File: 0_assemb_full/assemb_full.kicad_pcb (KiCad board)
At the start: 2 copper layers, 100.3 x 100.3 mm, 147 parts, among them J1 BarrelJack, J10 SPIConn_01x03, J11 OutToRPi, J2 Conn_02x06, J3 AudioJack3, J4 Servo0Conn_01x03, J5 Servo1Conn_01x03, J6 Servo2Conn_01x03, J7 Servo3Conn_01x03, J8 Servo4Conn_01x03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

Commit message: Pre-STM32 portion rework
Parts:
- added C50: 0.1u, Capacitor_SMD:C_0805_2012Metric_Pad1.18x1.45mm_HandSolder, B.Cu at (69.8, 100.0)
- added REF**: SolderJumper-2_P1.3mm_Open_Pad1.0x1.5mm, Jumper:SolderJumper-2_P1.3mm_Open_Pad1.0x1.5mm, F.Cu at (109.4, 113.2)
- added U7: MAX7375AXR805, Package_TO_SOT_SMD:SOT-323_SC-70, B.Cu at (67.4, 100.0)
- H1, H2, H3, H4: footprint MountingHole:MountingHole_6.4mm_M6 -> MountingHole:MountingHole_3.2mm_M3
- R5, R9: moved to B.Cu
- moved R3 247.7 mm to (13.6, 148.3)
- moved R2 247.7 mm to (23.5, 142.2)
- moved TP9 247.1 mm to (25.5, 149.0)
- moved TP7 205.9 mm to (45.9, 93.7)
- moved TP3 195.9 mm to (63.0, 115.7)
- moved TP1 188.3 mm to (60.3, 111.2)
- moved TP8 187.6 mm to (76.7, 145.1), turned to -90 degrees
- moved TP2 186.5 mm to (60.4, 115.3)
- moved TP5 184.0 mm to (57.6, 120.0)
- moved R8 178.4 mm to (79.0, 150.1), turned to 90 degrees
- moved TP4 175.2 mm to (60.5, 118.6)
- moved R5 173.8 mm to (70.8, 141.2), turned to -90 degrees
- moved R1 171.9 mm to (70.1, 144.9), turned to 180 degrees
- moved TP6 169.2 mm to (59.1, 108.5)
- moved R9 158.8 mm to (74.2, 139.8), turned to 180 degrees
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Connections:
- U5 pad 5: unconnected-(U5-Pad5) -> /STM32 Interface/EClock
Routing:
- net Filter_In: track 0.00 -> 29.7 mm
- net 5V: track 167.1 -> 194.0 mm
- net Audio_In_Ring: track 0.00 -> 21.5 mm
- net 3_3V: track 100.2 -> 119.2 mm
- net Net-(TP5-Pad1): track 0.00 -> 18.5 mm
- net ADC_LP: track 0.00 -> 17.9 mm
- net Net-(TP4-Pad1): track 0.00 -> 15.0 mm
- net ADC_BP: track 0.00 -> 14.6 mm
- net ADC_HP: track 0.00 -> 11.9 mm
- net GND: track 58.1 -> 69.7 mm, vias 4 -> 9
- net Audio_In_Tip: track 0.00 -> 11.5 mm
- net /Bandpass/LP Pre-LP: track 0.00 -> 10.7 mm
- net Net-(TP3-Pad1): track 0.00 -> 10.2 mm
- net Net-(C5-Pad2): track 0.00 -> 9.66 mm
- net Net-(C4-Pad2): track 0.00 -> 7.68 mm
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- added copper zone on F.Cu, net (none)
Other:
- board text added: "Change electrolytic to 0805"
- board text added: "Micro to the right Power and servo connections to the left"
- board text added: "Use two big vias instead of multiples"

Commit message: Additional changes
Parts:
- C13, C17, C19, C22, C23, C36, C37, C38, C39: footprint Capacitor_THT:CP_Radial_D5.0mm_P2.50mm -> Capacitor_SMD:C_0805_2012Metric_Pad1.18x1.45mm_HandSolder
- C2: footprint Capacitor_THT:CP_Radial_D5.0mm_P2.00mm -> Capacitor_SMD:C_0805_2012Metric_Pad1.18x1.45mm_HandSolder
- R10, R11, R6, R7: moved to B.Cu
- moved R11 206.9 mm to (61.4, 136.7)
- moved R7 194.5 mm to (65.6, 136.7)
- moved R6 183.2 mm to (88.6, 143.9)
- moved R10 169.8 mm to (84.6, 143.9)
- moved R3 67.4 mm to (80.9, 151.0), turned to 90 degrees
- moved TP9 67.0 mm to (92.5, 147.2)
- moved C3 63.7 mm to (90.8, 151.6), turned to 180 degrees
- moved R2 60.2 mm to (83.0, 151.1), turned to -90 degrees
- moved C7 60.0 mm to (81.5, 157.6)
- moved U4 6.15 mm to (91.5, 162.6)
- moved R1 4.91 mm to (70.1, 149.8)
- moved R23 4.91 mm to (59.5, 159.6)
- moved R5 4.91 mm to (70.8, 146.1)
- moved R8 4.91 mm to (79.1, 155.0)
- moved R9 4.91 mm to (74.2, 144.7)
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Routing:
- net Net-(C3-Pad1): track 0.00 -> 42.2 mm
- net Net-(C7-Pad2): track 0.00 -> 14.4 mm
- net 5V: track 194.0 -> 199.8 mm
- net Net-(R10-Pad2): track 0.00 -> 5.49 mm
- net Net-(R11-Pad2): track 0.00 -> 5.27 mm
- net Net-(C3-Pad2): track 0.00 -> 5.08 mm
- net /Bandpass/LP Pre-LP: track 10.7 -> 15.0 mm, vias 0 -> 1
- net Net-(R4-Pad1): track 0.00 -> 3.17 mm
- net GND: track 69.7 -> 67.5 mm, vias 9 -> 8
- net Audio_In_Ring: track 21.5 -> 23.6 mm

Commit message: Some filter adjustments
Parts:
- removed REF** (x2): SolderJumper-2_P1.3mm_Open_Pad1.0x1.5mm, Jumper:SolderJumper-2_P1.3mm_Open_Pad1.0x1.5mm
- added C51: 100n, Capacitor_SMD:C_0805_2012Metric_Pad1.18x1.45mm_HandSolder, F.Cu at (143.3, 124.4)
- added C52: 100n, Capacitor_SMD:C_0805_2012Metric_Pad1.18x1.45mm_HandSolder, F.Cu at (152.4, 124.4)
- added C53: 100n, Capacitor_SMD:C_0805_2012Metric_Pad1.18x1.45mm_HandSolder, F.Cu at (143.3, 130.8)
- FB1: moved to F.Cu
- J2: footprint Connector_PinSocket_2.54mm:PinSocket_2x06_P2.54mm_Vertical -> Connector_PinHeader_2.54mm:PinHeader_2x02_P2.54mm_Vertical
- J4, J5, J6, J7, J8: footprint Connector_PinSocket_2.54mm:PinSocket_1x03_P2.54mm_Vertical -> Connector_PinHeader_2.54mm:PinHeader_1x03_P2.54mm_Vertical
- J9: value Conn_02x05_Odd_Even -> ProgHeader
- moved U6 95.8 mm to (18.1, 165.1)
- moved J2 92.7 mm to (42.4, 97.0), turned to -90 degrees
- moved C12 91.0 mm to (128.4, 187.2)
- moved J9 52.6 mm to (131.3, 118.1)
- moved H3 51.8 mm to (70.9, 88.6)
- moved J10 47.8 mm to (87.1, 107.7), turned to -90 degrees
- moved J1 47.5 mm to (59.4, 100.2)
- moved SW1 46.3 mm to (84.5, 117.1)
- moved R32 46.1 mm to (103.2, 101.3)
- moved R36 46.1 mm to (103.7, 114.9)
- moved C14 46.1 mm to (110.6, 113.5)
- moved C15 46.1 mm to (117.1, 113.5)
- moved C16 46.1 mm to (110.0, 96.0)
- moved C18 46.1 mm to (121.8, 100.9)
- moved C21 46.1 mm to (98.4, 101.3)
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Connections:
- J2 pad 1: 5V -> 12V
- J2 pad 2: 5V -> GND
- J2 pad 3: GND -> 5V
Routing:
- net 5V: track 199.8 -> 101.9 mm, vias 1 -> 0
- net 3_3V: track 119.2 -> 34.2 mm, vias 2 -> 0
- net /STM32 Interface/SPI_SCK: track 45.2 -> 2.42 mm
- net /STM32 Interface/SPI_MOSI: track 44.2 -> 1.45 mm
- net /STM32 Interface/SPI_NSS: track 44.5 -> 2.47 mm
- net /STM32 Interface/NRST: track 45.3 -> 77.8 mm, vias 1 -> 0
- net 12VRP: track 105.2 -> 78.0 mm
- net 12V: track 38.5 -> 18.3 mm
- net ADC_LP: track 17.9 -> 0.00 mm
- net GND: track 67.5 -> 51.1 mm, vias 8 -> 4
- net ADC_BP: track 14.6 -> 0.42 mm
- net ADC_HP: track 11.9 -> 2.66 mm
- net /STM32 Interface/VDDA: track 40.2 -> 31.2 mm, vias 1 -> 2
- net /STM32 Interface/SWCLK_IN: track 25.8 -> 31.8 mm
- net /STM32 Interface/SWDIO_IN: track 21.0 -> 26.5 mm
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- added copper zone on F.Cu, net 3_3V
- removed copper zone on F.Cu, net GND

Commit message: Active Filters layout added
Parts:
- removed R12, R13, R14, R15, R16, R17, R18, R19: 220, Resistor_SMD:R_0805_2012Metric_Pad1.20x1.40mm_HandSolder
- added REF**: SolderJumper-2_P1.3mm_Open_Pad1.0x1.5mm, Jumper:SolderJumper-2_P1.3mm_Open_Pad1.0x1.5mm, F.Cu at (78.1, 107.9)
- added REF**: SolderJumper-2_P1.3mm_Open_Pad1.0x1.5mm, Jumper:SolderJumper-2_P1.3mm_Open_Pad1.0x1.5mm, B.Cu at (87.4, 130.8)
- added REF**: SolderJumper-2_P1.3mm_Open_Pad1.0x1.5mm, Jumper:SolderJumper-2_P1.3mm_Open_Pad1.0x1.5mm, B.Cu at (55.4, 130.5)
- added REF**: SolderJumper-2_P1.3mm_Open_Pad1.0x1.5mm, Jumper:SolderJumper-2_P1.3mm_Open_Pad1.0x1.5mm, B.Cu at (52.8, 130.5)
- added REF**: SolderJumper-2_P1.3mm_Open_Pad1.0x1.5mm, Jumper:SolderJumper-2_P1.3mm_Open_Pad1.0x1.5mm, B.Cu at (84.4, 130.8)
- C52, R22, R23, R24, R25, R27, R28, R30, R31: moved to B.Cu
- LS1, LS2, LS3, LS4: footprint Connector_Wire:SolderWire-2.5sqmm_1x02_P7.2mm_D2.4mm_OD3.6mm -> Connector_Wire:SolderWire-2sqmm_1x02_P7.8mm_D2mm_OD3.9mm
- moved L1 198.7 mm to (-13.0, 181.2)
- moved L3 198.7 mm to (20.7, 163.1)
- moved L4 198.7 mm to (-15.4, 192.3)
- moved L5 198.7 mm to (0.33, 174.5)
- moved L6 198.7 mm to (9.64, 163.1)
- moved LS4 180.7 mm to (41.4, 173.3), turned to 90 degrees
- moved LS1 178.6 mm to (72.0, 187.6), turned to 180 degrees
- moved LS2 177.3 mm to (56.1, 187.6), turned to 180 degrees
- moved R38 174.7 mm to (54.9, 146.0), turned to -90 degrees
- moved R37 166.7 mm to (59.9, 145.0), turned to -90 degrees
- moved R4 165.3 mm to (96.5, 142.8), turned to 180 degrees
- moved JP1 163.3 mm to (52.2, 138.6)
- moved L2 162.1 mm to (13.0, 182.4)
- moved LS3 161.8 mm to (41.4, 187.5), turned to 90 degrees
- moved C37 149.6 mm to (65.2, 153.2), turned to 180 degrees
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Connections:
- C23 pad 1: 12VRP -> 12V
- C29 pad 1: 12VRP -> 12V
- C30 pad 1: 12VRP -> 12V
- C31 pad 1: 12VRP -> 12V
- C33 pad 1: 12VRP -> 12V
- C34 pad 1: 12VRP -> 12V
- C35 pad 1: 12VRP -> 12V
- R41 pad 1: 12VRP -> 12V
- R42 pad 1: 12VRP -> 12V
- U6 pad 15: 12VRP -> 12V
- U6 pad 16: 12VRP -> 12V
- U6 pad 27: 12VRP -> 12V
- U6 pad 28: 12VRP -> 12V
- U6 pad 7: 12VRP -> 12V
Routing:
- net 5V: track 101.9 -> 255.4 mm, vias 0 -> 3
- net 12V: track 18.3 -> 144.8 mm, vias 0 -> 3
- net ADC_LP: track 0.00 -> 104.6 mm, vias 0 -> 3
- net 3_3V: track 34.2 -> 137.1 mm, vias 0 -> 4
- net 12VRP: track 78.0 -> 0.00 mm
- net SERVO3: track 24.7 -> 85.6 mm, vias 2 -> 1
- net Filter_In: track 29.7 -> 88.5 mm
- net SERVO2: track 25.5 -> 82.5 mm, vias 2 -> 1
- net SERVO1: track 27.4 -> 79.5 mm, vias 2 -> 1
- net SERVO0: track 31.3 -> 80.1 mm, vias 2 -> 1
- net ADC_BP: track 0.42 -> 43.3 mm, vias 0 -> 1
- net Audio_In_Tip: track 11.4 -> 53.9 mm
- net Audio_In_Ring: track 23.6 -> 64.9 mm
- net GND: track 51.1 -> 90.7 mm, vias 4 -> 24
- net Net-(C8-Pad1): track 0.00 -> 37.3 mm
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- added copper zone on F.Cu, net GND
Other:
- board text removed: "Change electrolytic to 0805"
- board text removed: "Micro to the right Power and servo connections to the left"
- board text removed: "Use two big vias instead of multiples"

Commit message: Full PCB layout complete
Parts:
- C22, C23, C36, C42, C43, C44, C45, C46, C47, C48, C49, R39, R40, R43, R44, R45, R46: moved to B.Cu
- moved C45 195.9 mm to (62.8, 169.3)
- moved R43 192.8 mm to (67.0, 171.4), turned to 180 degrees
- moved C42 191.2 mm to (49.3, 166.6), turned to 180 degrees
- moved C41 185.2 mm to (53.8, 180.3), turned to -90 degrees
- moved C46 185.0 mm to (62.8, 171.4)
- moved FB2 179.4 mm to (61.8, 165.7), turned to 90 degrees
- moved C36 179.3 mm to (60.8, 154.3), turned to 90 degrees
- moved FB3 172.2 mm to (57.9, 165.7), turned to 90 degrees
- moved C31 171.9 mm to (73.4, 157.8)
- moved C29 170.5 mm to (67.3, 158.7), turned to -90 degrees
- moved C40 167.3 mm to (58.8, 174.9), turned to -90 degrees
- moved C26 167.2 mm to (88.9, 179.6)
- moved C33 164.1 mm to (53.1, 155.7), turned to 90 degrees
- moved C30 164.0 mm to (69.6, 155.4), turned to 90 degrees
- moved C44 163.8 mm to (56.9, 169.3), turned to 180 degrees
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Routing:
- net Net-(C44-Pad1): track 0.00 -> 43.4 mm, vias 0 -> 1
- net Net-(C26-Pad1): track 0.00 -> 35.4 mm, vias 0 -> 1
- net Net-(C40-Pad1): track 0.00 -> 30.5 mm, vias 0 -> 1
- net Net-(C45-Pad1): track 0.00 -> 25.2 mm, vias 0 -> 1
- net Net-(L5-Pad2): track 0.00 -> 23.1 mm
- net 12V: track 144.8 -> 167.7 mm, vias 3 -> 2
- net Net-(L2-Pad2): track 0.00 -> 19.7 mm
- net Net-(C41-Pad2): track 0.00 -> 13.2 mm
- net Net-(L1-Pad2): track 0.00 -> 12.7 mm
- net Net-(C27-Pad2): track 0.00 -> 9.67 mm
- net Net-(C32-Pad1): track 0.00 -> 9.62 mm
- net Net-(R42-Pad2): track 0.00 -> 9.42 mm
- net Net-(L4-Pad2): track 0.00 -> 9.39 mm
- net Net-(C28-Pad1): track 0.00 -> 9.05 mm
- net Net-(C25-Pad2): track 0.00 -> 8.86 mm
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
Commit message: Final adjustments
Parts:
- added J12: LEDConn_01x05, Connector_PinHeader_2.54mm:PinHeader_1x05_P2.54mm_Vertical, F.Cu at (98.8, 185.8)
- added J13: RPiConn_01x03, Connector_PinSocket_2.54mm:PinSocket_1x03_P2.54mm_Vertical, F.Cu at (127.7, 94.5)
- moved TP7 7.16 mm to (126.7, 112.2)
- moved R34 3.04 mm to (117.1, 94.5), turned to -90 degrees
- moved J10 1.57 mm to (122.6, 119.9)
- moved L3 0.95 mm to (68.5, 175.5)
- moved C9 0.30 mm to (107.3, 178.3)
- turned H2 to 180 degrees
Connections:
- U5 pad 59: unconnected-(U5-Pad59) -> /STM32 Interface/GPIO1
- U5 pad 61: unconnected-(U5-Pad61) -> /STM32 Interface/GPIO2
- U5 pad 62: unconnected-(U5-Pad62) -> /STM32 Interface/GPIO3
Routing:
- net ADC_HP: track 37.0 -> 158.1 mm
- net ADC_BP: track 43.3 -> 88.7 mm, vias 1 -> 4
- net Net-(C45-Pad1): track 25.2 -> 54.2 mm
- net 5V: track 252.3 -> 278.9 mm
- net /STM32 Interface/GPIO2: track 0.00 -> 18.1 mm, vias 0 -> 2
- net /STM32 Interface/GPIO1: track 0.00 -> 17.5 mm
- net /STM32 Interface/GPIO3: track 0.00 -> 13.9 mm
- net Audio_In_Tip: track 48.3 -> 60.9 mm
- net /STM32 Interface/NRST: track 75.4 -> 87.3 mm
- net ADC_LP: track 104.6 -> 112.7 mm
- net 3_3V: track 137.1 -> 144.8 mm
- net GND: track 92.0 -> 95.3 mm, vias 29 -> 30
- net /STM32 Interface/SPI_MOSI: track 14.5 -> 16.6 mm
- net /STM32 Interface/SPI_SCK: track 14.6 -> 13.0 mm
- net /STM32 Interface/SPI_NSS: track 14.6 -> 13.1 mm
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
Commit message: Final changes to PCB after footprint tests.
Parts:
- added REF**: SolderJumper-2_P1.3mm_Open_Pad1.0x1.5mm, Jumper:SolderJumper-2_P1.3mm_Open_Pad1.0x1.5mm, B.Cu at (94.7, 93.6)
- J1: footprint Connector_BarrelJack:BarrelJack_CUI_PJ-102AH_Horizontal -> Connector_BarrelJack:BarrelJack_GCT_DCJ200-10-A_Horizontal
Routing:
- net GND: track 95.3 -> 97.0 mm
- net 3_3V: track 144.8 -> 144.0 mm
- net 12V: track 167.7 -> 168.3 mm

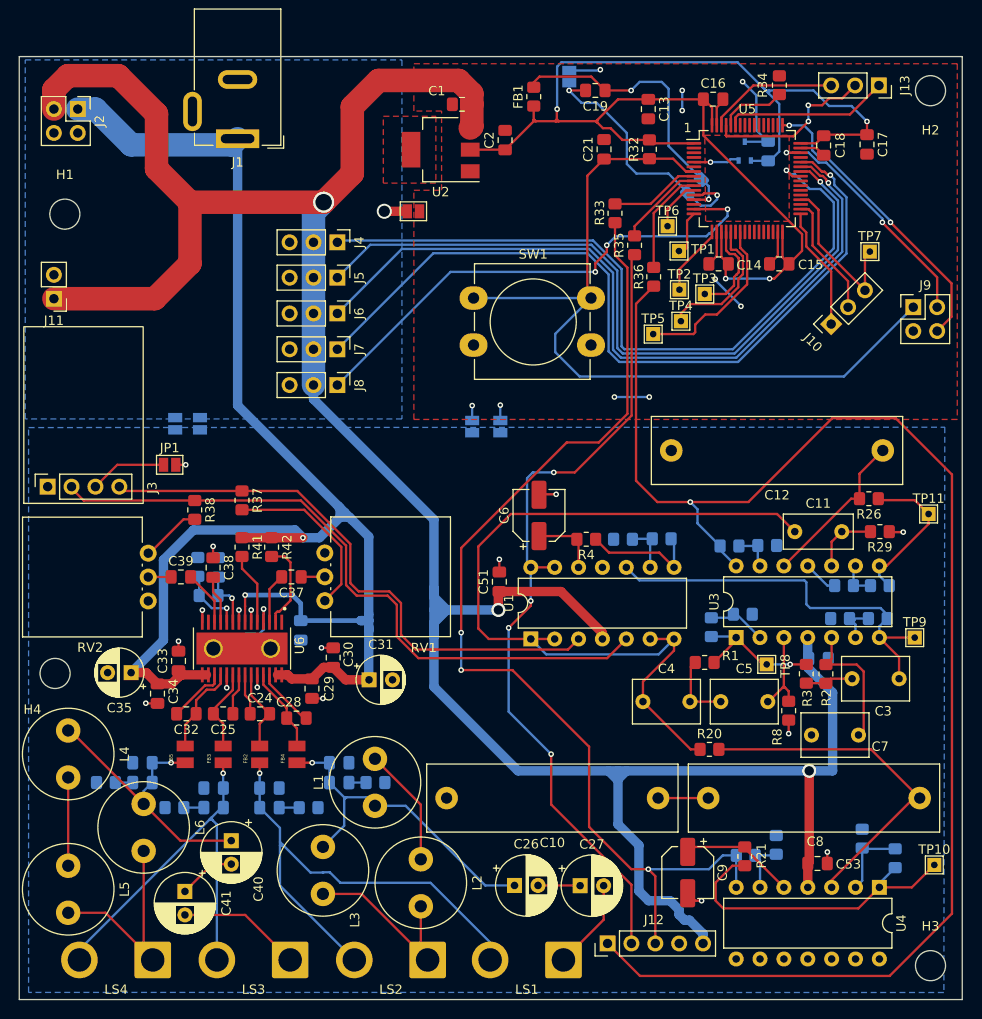
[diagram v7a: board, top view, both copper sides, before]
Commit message: Final adjustments (mostly silkscreen) pre-presentation
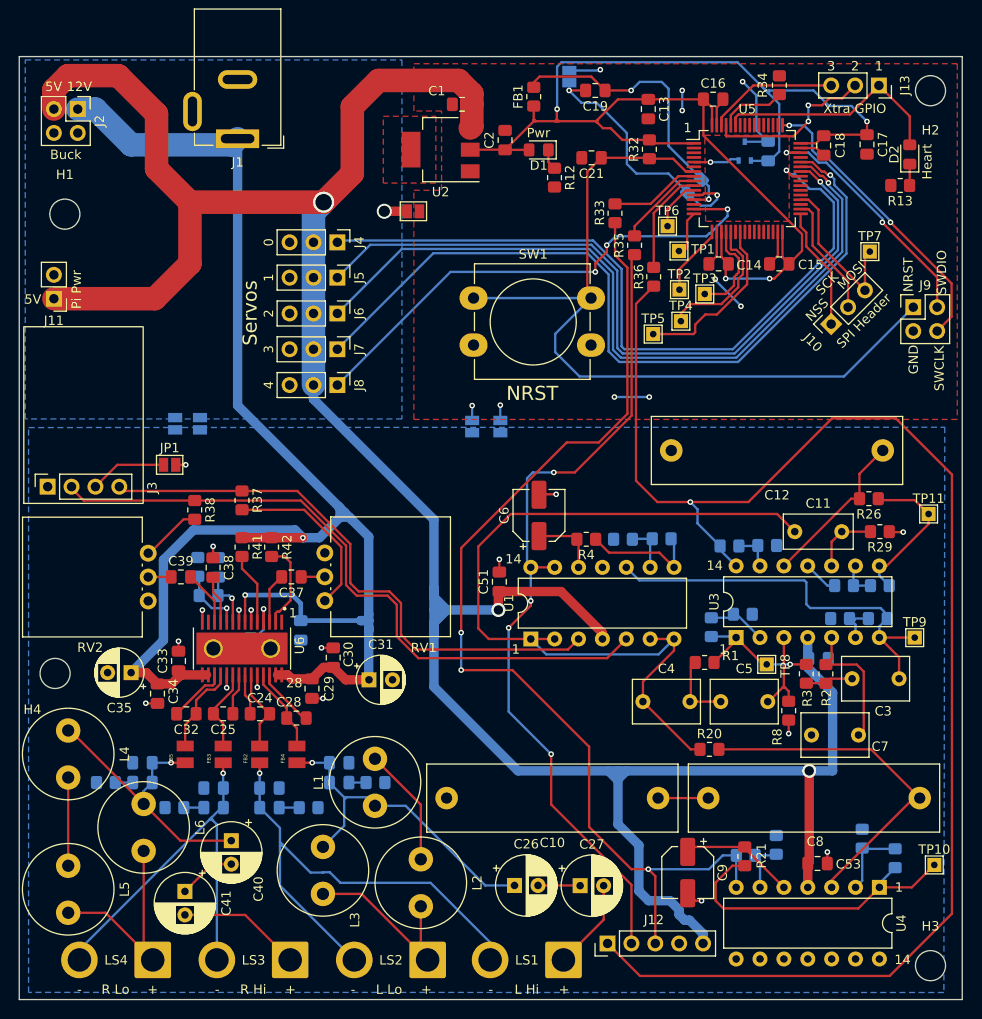
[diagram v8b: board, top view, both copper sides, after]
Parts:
- added D1: LED, LED_SMD:LED_0805_2012Metric_Pad1.15x1.40mm_HandSolder, F.Cu at (91.5, 101.4)
- added D2: LED, LED_SMD:LED_0805_2012Metric_Pad1.15x1.40mm_HandSolder, F.Cu at (130.9, 101.9)
- added R12: 200, Resistor_SMD:R_0805_2012Metric_Pad1.20x1.40mm_HandSolder, F.Cu at (93.1, 104.3)
- added R13: 200, Resistor_SMD:R_0805_2012Metric_Pad1.20x1.40mm_HandSolder, F.Cu at (129.9, 105.2)
- moved C21 1.61 mm to (97.1, 102.2), turned to 180 degrees
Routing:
- net /STM32 Interface/GPIO1: track 17.5 -> 25.2 mm
- net 3_3V: track 144.0 -> 146.5 mm
- net Net-(D2-Pad1): track 0.00 -> 2.28 mm
- net Net-(D1-Pad1): track 0.00 -> 2.22 mm
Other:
- board text added: "+"
- board text added: "-"
- board text added: "0"
- board text added: "12V"
- board text added: "14"
- board text added: "2"
- board text added: "28"
- board text added: "3"
- board text added: "4"
- board text added: "5V"
- board text added: "Buck"
- board text added: "ECE477 Team 10 Julian Kang, Lydia Allen, Ryan Davitt, Vivek Panchagnula Main Board (REV1.0, 2-27-2024)"
- board text added: "GND"
- board text added: "Heart"
- board text added: "L Hi"
- board text added: "L Lo"
- board text added: "MOSI"
- board text added: "NRST"
- board text added: "NSS"
- board text added: "Pi Pwr"
- board text added: "Pwr"
- board text added: "R Hi"
- board text added: "R Lo"
- board text added: "SCK"
- board text added: "SPI Header"
- board text added: "SWCLK"
- board text added: "SWDIO"
- board text added: "Servos"
- board text added: "Xtra GPIO"
